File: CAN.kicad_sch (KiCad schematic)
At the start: 18 parts, among them U3 ISO1044BD, U4 UCC12050DVE

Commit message: Updated Params
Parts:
- D1: value D_TVS -> RLSD32A241LC
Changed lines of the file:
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@@
 		(on_board yes)
 		(dnp no)
-		(fields_autoplaced yes)
 		(property "Reference" "#PWR030"
 			(at 68.58 138.43 0)
@@
 		)
 		(property "Value" "CAN_GND"
-			(at 71.12 133.1594 0)
+			(at 64.516 135.636 0)
 			(effects
 				(font
@@
 			)
 		)
-		(property "Value" "D_TVS"
+		(property "Value" "RLSD32A241LC"
 			(at 64.77 64.7699 90)
 			(effects

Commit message: Updated Hierarchical Labels
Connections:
- net CAN_5VIN: no longer C27.1, C28.1, U4.13 (SEL), U4.14 (VISO)
- net CAN1_RX renamed CAN_RX
- net CAN1_TX renamed CAN_TX
- new net CAN_5VOUT: C27.1, C28.1, U4.13 (SEL), U4.14 (VISO)
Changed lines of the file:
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@@
 	(wire
 		(pts
-			(xy 227.33 68.58) (xy 232.41 68.58)
+			(xy 227.33 68.58) (xy 242.57 68.58)
 		)
 		(stroke
@@
 	(wire
 		(pts
-			(xy 256.54 63.5) (xy 261.62 63.5)
+			(xy 256.54 63.5) (xy 269.24 63.5)
 		)
 		(stroke
@@
 	(wire
 		(pts
-			(xy 227.33 66.04) (xy 232.41 66.04)
+			(xy 227.33 66.04) (xy 242.57 66.04)
 		)
 		(stroke
@@
 		)
 	)
-	(hierarchical_label "CAN_5VIN"
+	(hierarchical_label "CAN_5VOUT"
 		(shape output)
 		(at 149.86 137.16 0)
@@
 	)
 	(hierarchical_label "CAN_5VIN"
+		(shape output)
+		(at 46.99 165.1 180)
+		(effects
+			(font
+				(size 1.27 1.27)
+			)
+			(justify right)
+		)
+	)
+	(hierarchical_label "CAN_RX"
+		(shape output)
+		(at 242.57 66.04 0)
+		(effects
+			(font
+				(size 1.27 1.27)
+			)
+			(justify left)
+		)
+	)
+	(hierarchical_label "PWR_3V3"
 		(shape input)
-		(at 46.99 165.1 180)
-		(effects
-			(font
-				(size 1.27 1.27)
-			)
-			(justify right)
-		)
-	)
+		(at 269.24 63.5 0)
+		(effects
+			(font
+				(size 1.27 1.27)
+			)
+			(justify left)
+		)
+	)
+	(hierarchical_label "CAN_TX"
+		(shape input)
+		(at 242.57 68.58 0)
+		(effects
+			(font
+				(size 1.27 1.27)
+			)
+			(justify left)
+		)
+	)

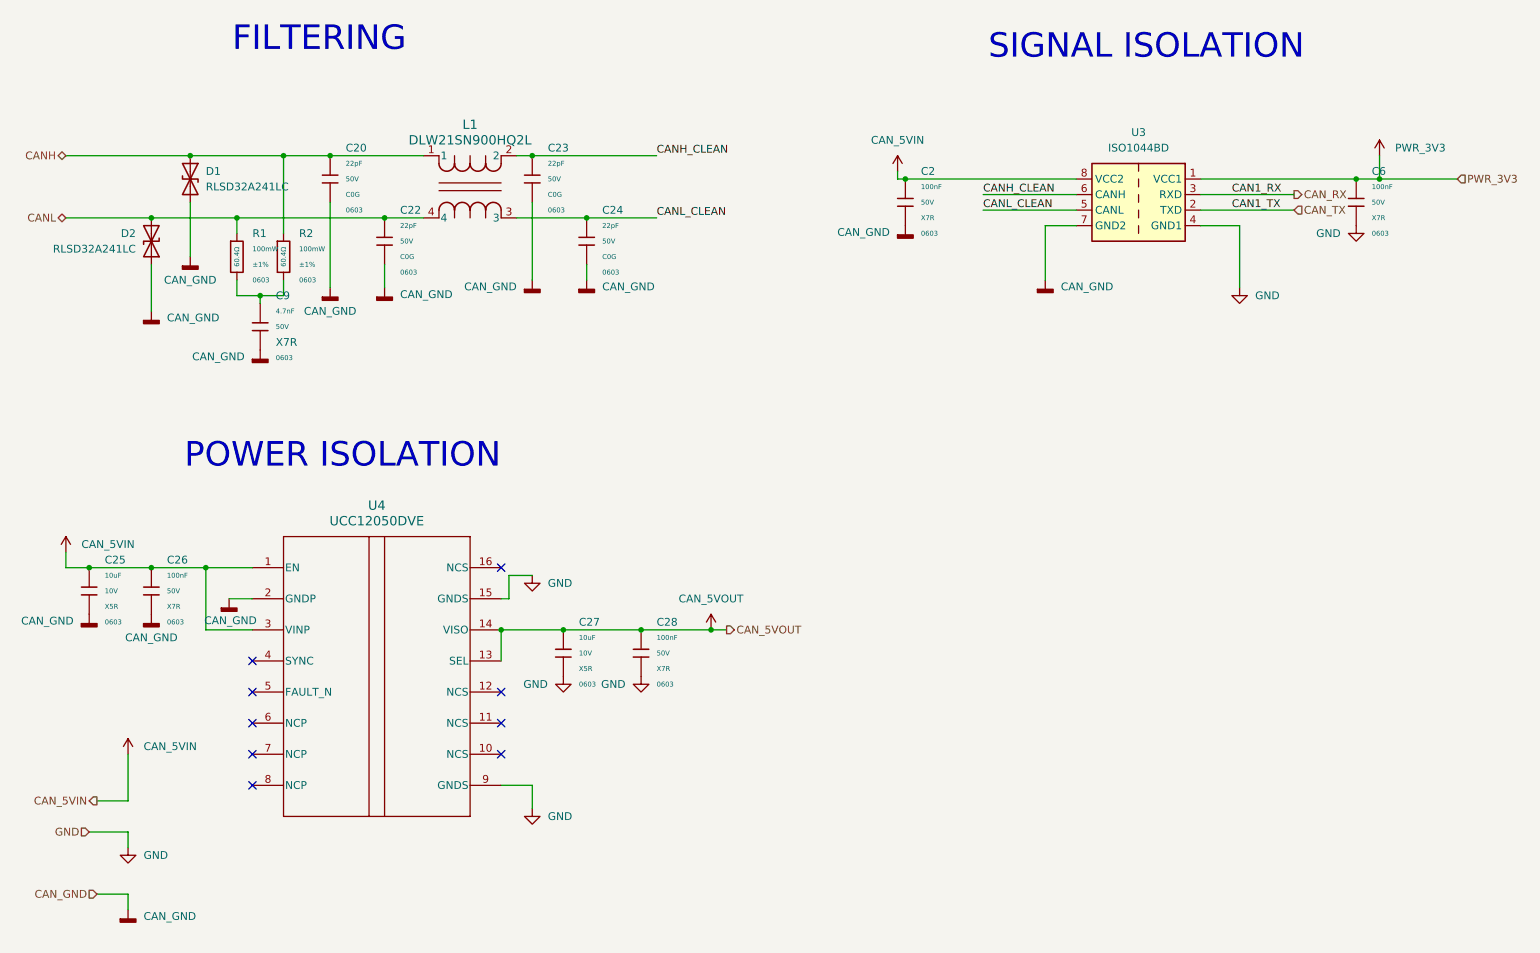
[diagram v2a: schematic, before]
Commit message: Fixed ERC errors and updated schem layout
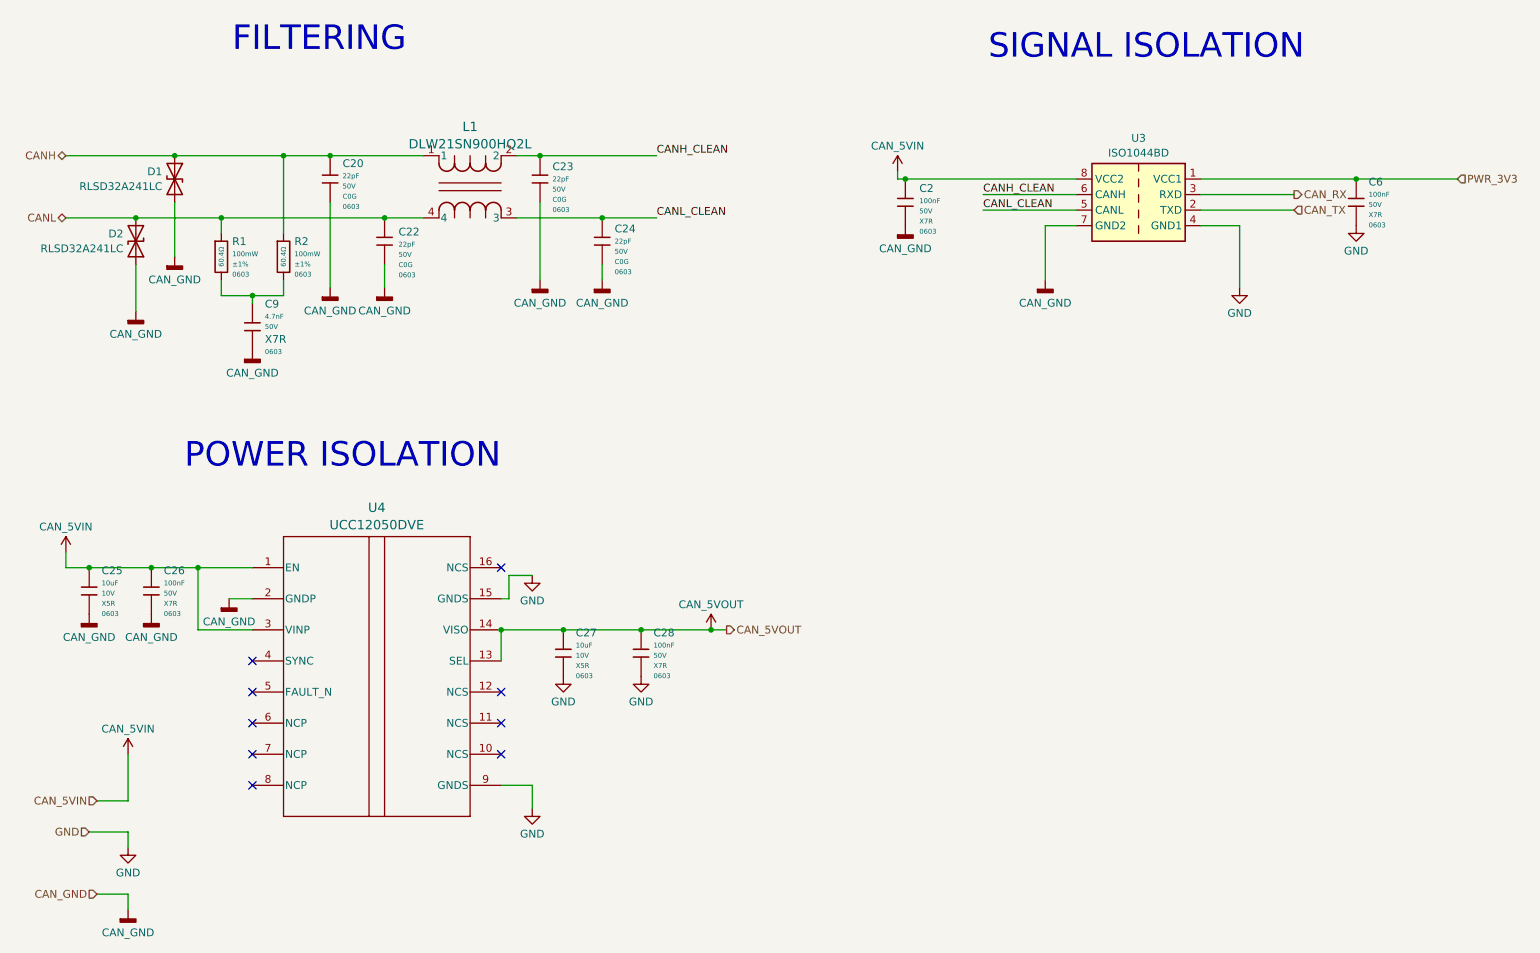
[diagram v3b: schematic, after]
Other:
- moved on the sheet: C23, C24, C9, D1, D2, R1
